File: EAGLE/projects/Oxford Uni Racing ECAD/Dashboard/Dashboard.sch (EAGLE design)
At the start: 22 parts, among them J1 T821108A1S100CEU, J2 CAN_OUT, J3 PWR_CAN, J4 DISPL, J6 BUTTONS, J7 BUTTONS, K1 EC2-12NU, K2 EC2-12NU, X2 D-SUB9-H2M09ST

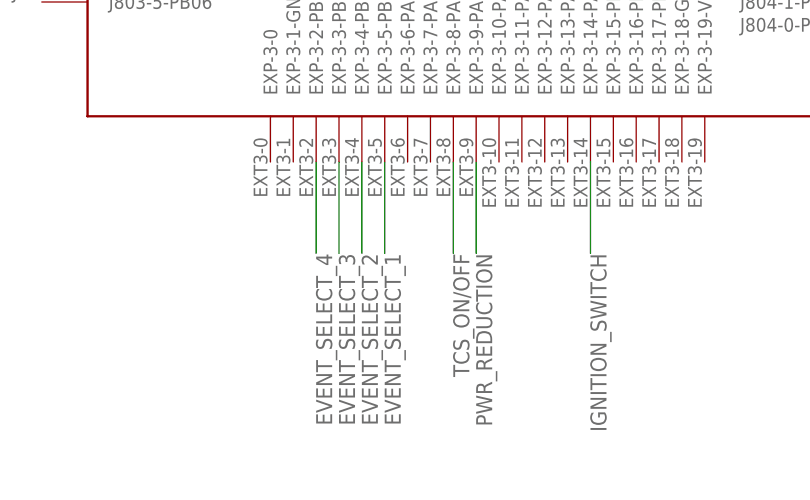
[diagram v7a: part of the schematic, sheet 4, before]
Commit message: fixed overlapping digital pins
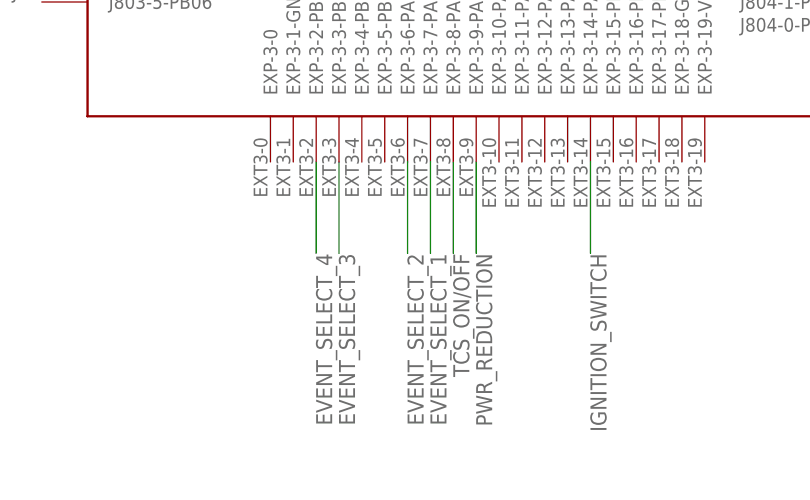
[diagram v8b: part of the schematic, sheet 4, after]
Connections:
- net EVENT_SELECT_1: now also U$1.EXP-3-7-PA15; no longer U$1.EXP-3-5-PB05
- net EVENT_SELECT_2: now also U$1.EXP-3-6-PA14; no longer U$1.EXP-3-4-PB04
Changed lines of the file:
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@@
 </segment>
 <segment>
-<label x="200.66" y="-17.78" size="1.778" layer="95" rot="R270"/>
-<wire x1="200.66" y1="-17.78" x2="200.66" y2="-7.62" width="0.1524" layer="91"/>
-<pinref part="U$1" gate="G$1" pin="EXP-3-5-PB05"/>
+<pinref part="U$1" gate="G$1" pin="EXP-3-7-PA15"/>
+<wire x1="205.74" y1="-7.62" x2="205.74" y2="-17.78" width="0.1524" layer="91"/>
+<label x="205.74" y="-17.78" size="1.778" layer="95" rot="R270"/>
 </segment>
 </net>
@@
 </segment>
 <segment>
-<label x="198.12" y="-17.78" size="1.778" layer="95" rot="R270"/>
-<wire x1="198.12" y1="-17.78" x2="198.12" y2="-7.62" width="0.1524" layer="91"/>
-<pinref part="U$1" gate="G$1" pin="EXP-3-4-PB04"/>
+<pinref part="U$1" gate="G$1" pin="EXP-3-6-PA14"/>
+<wire x1="203.2" y1="-7.62" x2="203.2" y2="-17.78" width="0.1524" layer="91"/>
+<label x="203.2" y="-17.78" size="1.778" layer="95" rot="R270"/>
 </segment>
 </net>
